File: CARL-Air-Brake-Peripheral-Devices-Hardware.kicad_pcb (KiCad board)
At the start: 2 copper layers, 65 x 56 mm, 53 parts, among them J1 ICSP, J2 USB, J3 Raspberry Pi, J4 Servo power, J5 Servo port, P1 BMP388, P2 BMP388, P3 BNO055, P4 BNO055, Q1 BSS138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

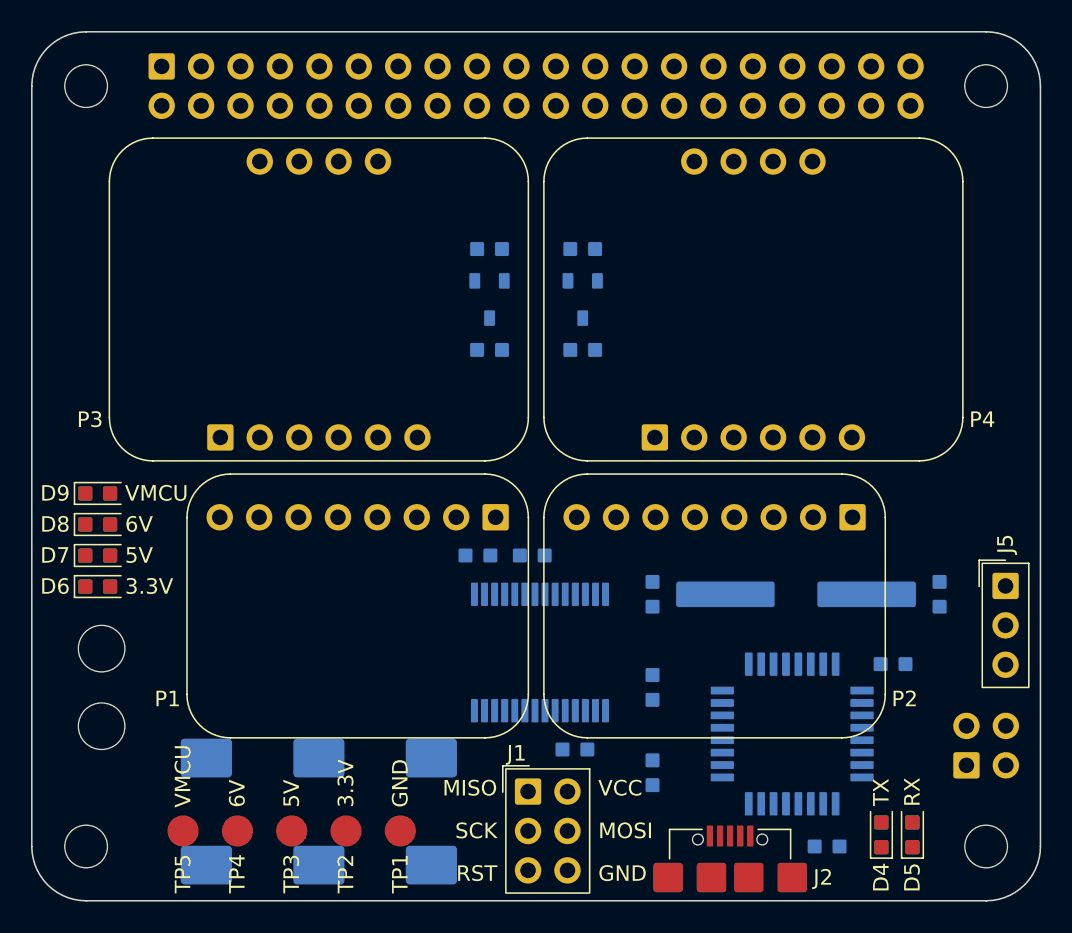
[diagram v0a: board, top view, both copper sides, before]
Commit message: Added filled zones
Added filled copper zones for high current power supply lines.
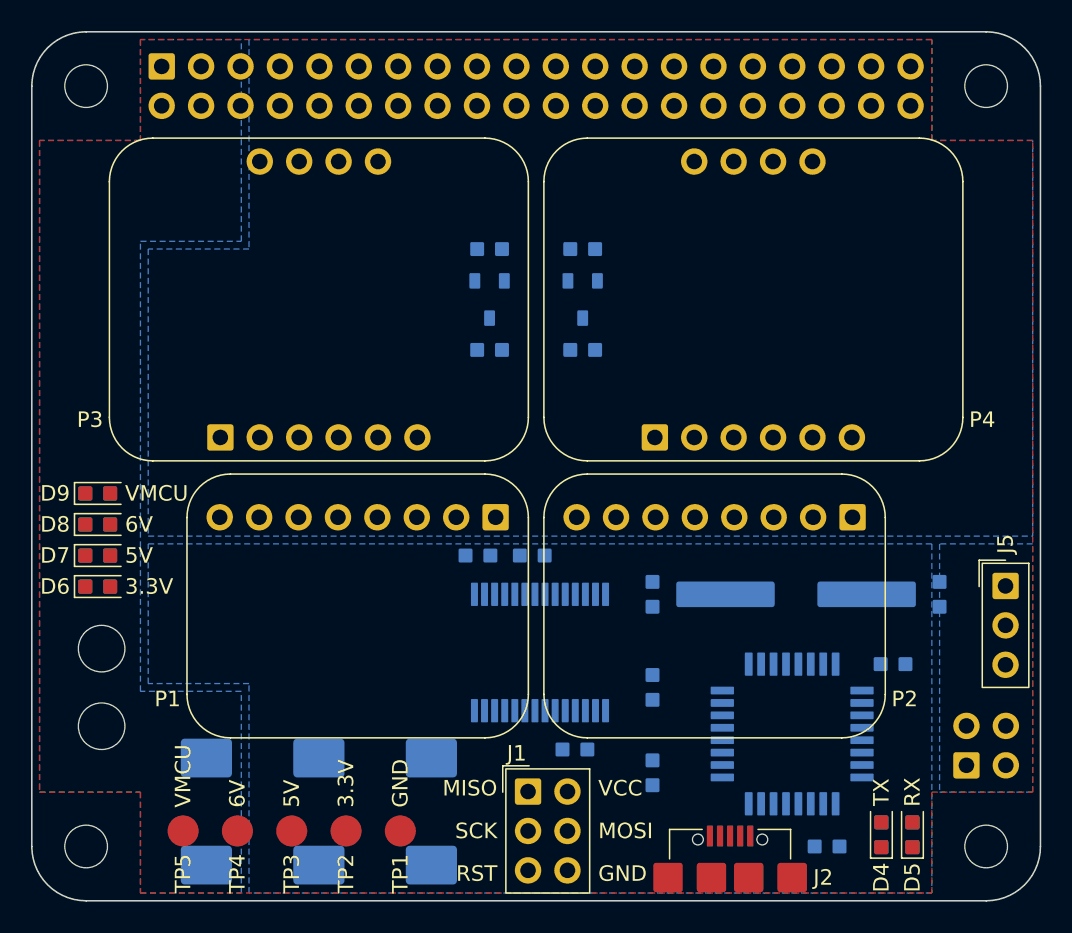
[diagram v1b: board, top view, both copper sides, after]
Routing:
- added copper zone on B.Cu, net +3.3V
- added copper zone on B.Cu, net +5V
- added copper zone on B.Cu, net +6V
- added copper zone on F.Cu, net GND
- added copper zone on B.Cu, net VMCU
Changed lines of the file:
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@@
       (stroke (width 0.05) (type default)) (fill none) (layer "F.CrtYd"))
     (pad "" np_thru_hole circle (at 0 0) (size 3 3) (drill 3) (layers "F&B.Cu" "*.Mask")
-      (solder_mask_margin 0.5))
+      (solder_mask_margin 0.5) (clearance 0.7))
   )
   (footprint "Local_LED_SMD:LED_0603" (layer "F.Cu")
@@
       (stroke (width 0.05) (type default)) (fill none) (layer "F.CrtYd"))
     (pad "" np_thru_hole circle (at 0 0) (size 3 3) (drill 3) (layers "F&B.Cu" "*.Mask")
-      (solder_mask_margin 0.5))
+      (solder_mask_margin 0.5) (clearance 0.7))
   )
   (footprint "Local_LED_SMD:LED_0603" (layer "F.Cu")
@@
     (style (thickness 0.1) (arrow_length 1) (text_position_mode 2) (extension_height 0.58642) (extension_offset 0) keep_text_aligned)
   )
+  (zone (net 1) (net_name "GND") (layer "F.Cu") (name "GND") (hatch edge 0.5)
+    (priority 4)
+    (connect_pads (clearance 0.2))
+    (min_thickness 0.2) (filled_areas_thickness no)
+    (fill (thermal_gap 0.2) (thermal_bridge_width 0.4) (smoothing fillet) (radius 0.5))
+    (polygon
+      (pts
+        (xy 124.5 72.5)
+        (xy 124.5 79)
+        (xy 118 79)
+        (xy 118 121)
+        (xy 124.5 121)
+        (xy 124.5 127.5)
+        (xy 175.5 127.5)
+        (xy 175.5 121)
+        (xy 182 121)
+        (xy 182 79)
+        (xy 175.5 79)
+        (xy 175.5 72.5)
+      )
+    )
+  )
+  (zone (net 18) (net_name "+6V") (layer "B.Cu") (name "+6V") (hatch edge 0.5)
+    (priority 2)
+    (connect_pads (clearance 0.2))
+    (min_thickness 0.2) (filled_areas_thickness no)
+    (fill (thermal_gap 0.2) (thermal_bridge_width 0.4) (smoothing fillet) (radius 0.5))
+    (polygon
+      (pts
+        (xy 182 105)
+        (xy 176 105)
+        (xy 176 121)
+        (xy 182 121)
+      )
+    )
+  )
+  (zone (net 2) (net_name "VMCU") (layer "B.Cu") (name "VMCU") (hatch edge 0.5)
+    (priority 3)
+    (connect_pads (clearance 0.2))
+    (min_thickness 0.2) (filled_areas_thickness no)
+    (fill (thermal_gap 0.2) (thermal_bridge_width 0.4) (smoothing fillet) (radius 0.5))
+    (polygon
+      (pts
+        (xy 175.5 105)
+        (xy 175.5 127.5)
+        (xy 131.5 127.5)
+        (xy 131.5 114)
+        (xy 125 114)
+        (xy 125 105)
+      )
+    )
+  )
+  (zone (net 15) (net_name "+3.3V") (layer "B.Cu") (name "+3.3V") (hatch edge 0.5)
+    (priority 1)
+    (connect_pads (clearance 0.2))
+    (min_thickness 0.2) (filled_areas_thickness no)
+    (fill (thermal_gap 0.2) (thermal_bridge_width 0.4) (smoothing fillet) (radius 0.5))
+    (polygon
+      (pts
+        (xy 131.5 72.5)
+        (xy 131.5 86)
+        (xy 125 86)
+        (xy 125 104.5)
+        (xy 182 104.5)
+        (xy 182 79)
+        (xy 175.5 79)
+        (xy 175.5 72.5)
+      )
+    )
+  )
+  (zone (net 8) (net_name "+5V") (layer "B.Cu") (name "+5V") (hatch edge 0.5)
+    (connect_pads (clearance 0.2))
+    (min_thickness 0.2) (filled_areas_thickness no)
+    (fill (thermal_gap 0.2) (thermal_bridge_width 0.4) (smoothing fillet) (radius 0.5))
+    (polygon
+      (pts
+        (xy 124.5 72.5)
+        (xy 124.5 79)
+        (xy 118 79)
+        (xy 118 121)
+        (xy 124.5 121)
+        (xy 124.5 127.5)
+        (xy 131 127.5)
+        (xy 131 114.5)
+        (xy 124.5 114.5)
+        (xy 124.5 85.5)
+        (xy 131 85.5)
+        (xy 131 72.5)
+      )
+    )
+  )
 )

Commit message: Routed circuit board
Completed circuit design by routing all connections, and performed DRC.
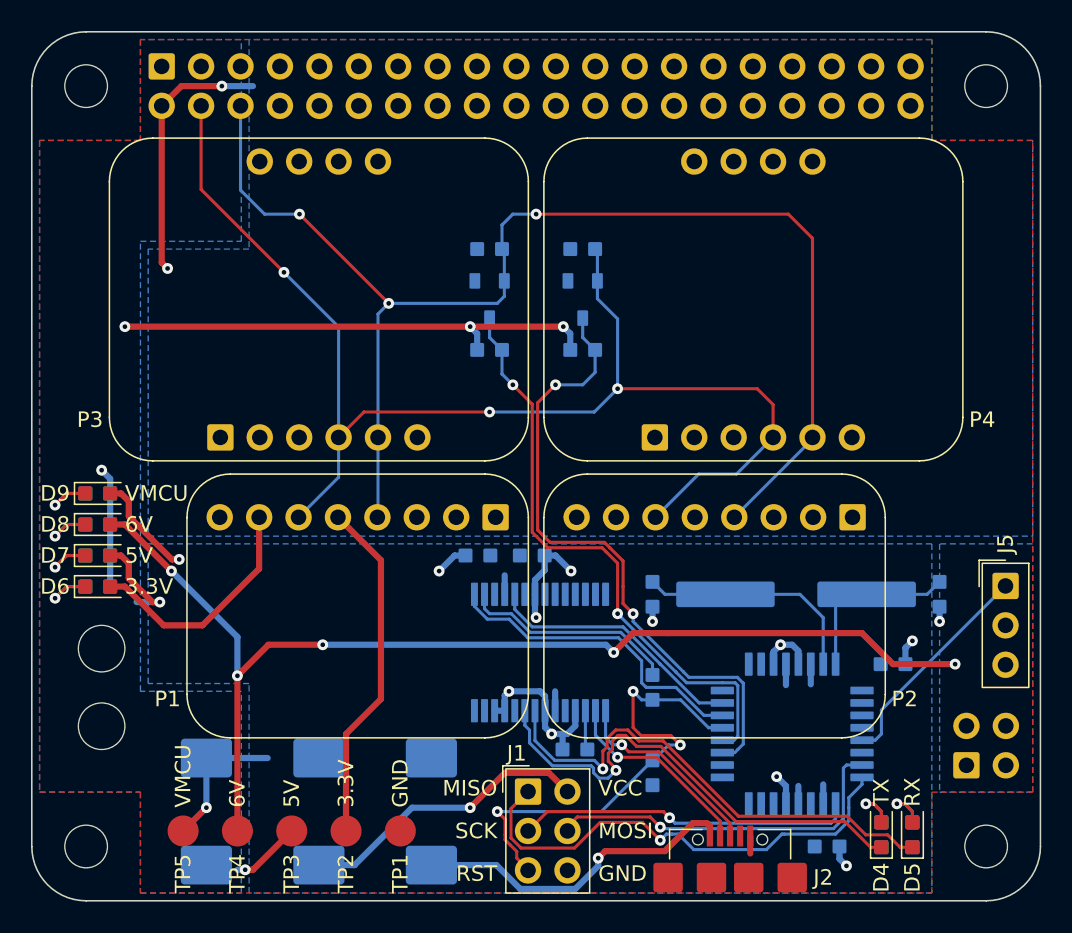
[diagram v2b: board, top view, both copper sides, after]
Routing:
- net /SCL_3.3V: track 0.00 -> 85.4 mm, vias 0 -> 3
- net /SDA_3.3V: track 0.00 -> 82.4 mm, vias 0 -> 3
- net +6V: track 0.00 -> 72.3 mm, vias 0 -> 5
- net +3.3V: track 0.00 -> 54.8 mm, vias 0 -> 2
- net +5V: track 0.00 -> 42.7 mm, vias 0 -> 5
- net /SDA_5V: track 0.00 -> 41.3 mm, vias 0 -> 2
- net GND: track 0.00 -> 38.8 mm, vias 0 -> 12
- net /SCL_5V: track 0.00 -> 38.6 mm, vias 0 -> 2
- net Net-(D5-K): track 0.00 -> 32.2 mm, vias 0 -> 1
- net Net-(D4-K): track 0.00 -> 31.8 mm, vias 0 -> 1
- net /ICSP_MISO: track 0.00 -> 31.1 mm, vias 0 -> 1
- net /ICSP_RESET: track 0.00 -> 30.7 mm, vias 0 -> 3
- net VMCU: track 0.00 -> 23.6 mm, vias 0 -> 2
- net /ICSP_MOSI: track 0.00 -> 23.4 mm, vias 0 -> 1
- net /ICSP_SCK: track 0.00 -> 21.8 mm, vias 0 -> 1
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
